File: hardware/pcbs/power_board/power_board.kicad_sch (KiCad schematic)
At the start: 5 parts, among them J1 Header_01x04

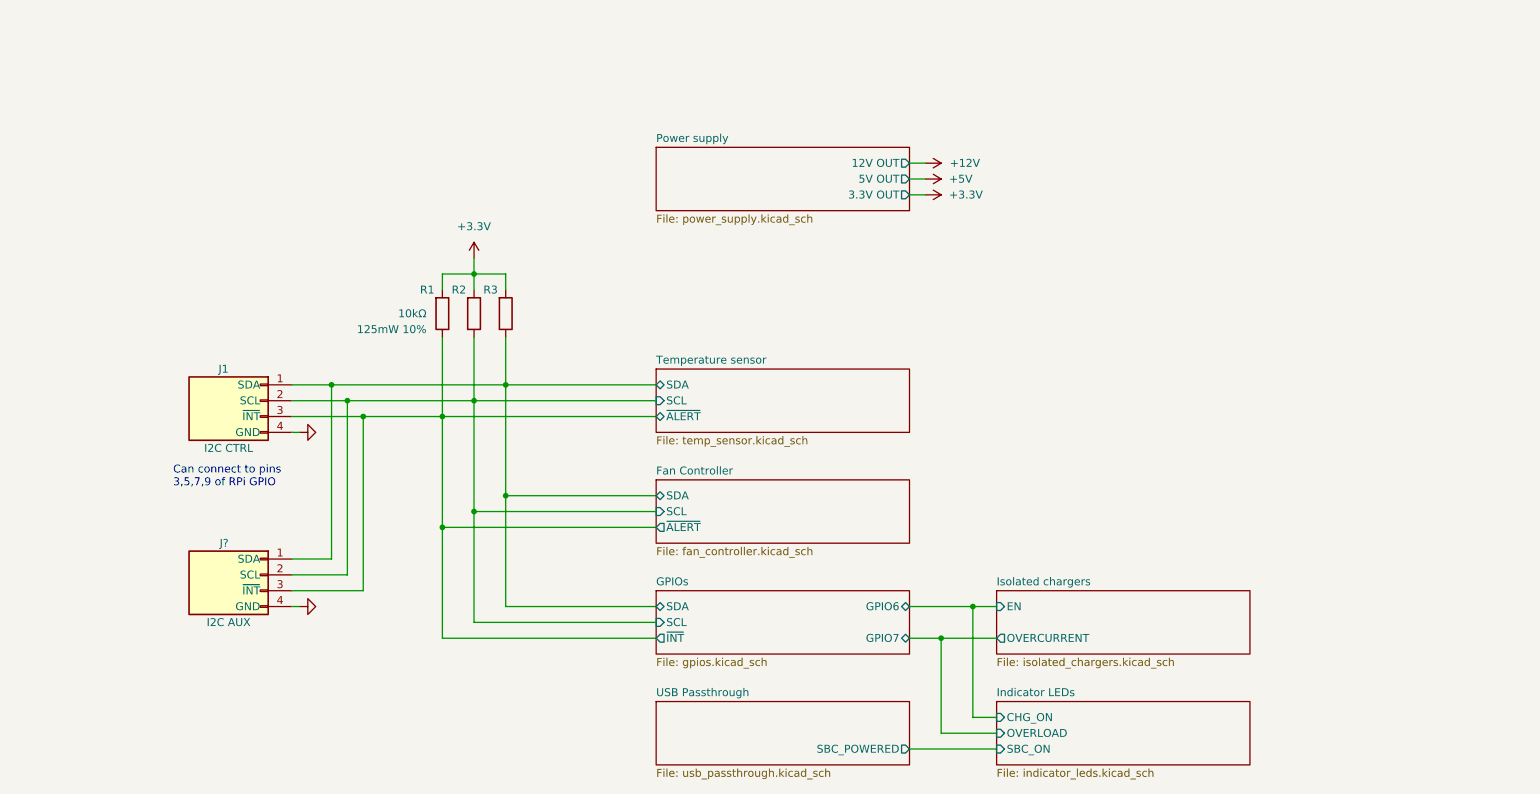
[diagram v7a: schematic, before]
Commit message: power_board: arrange front panel components
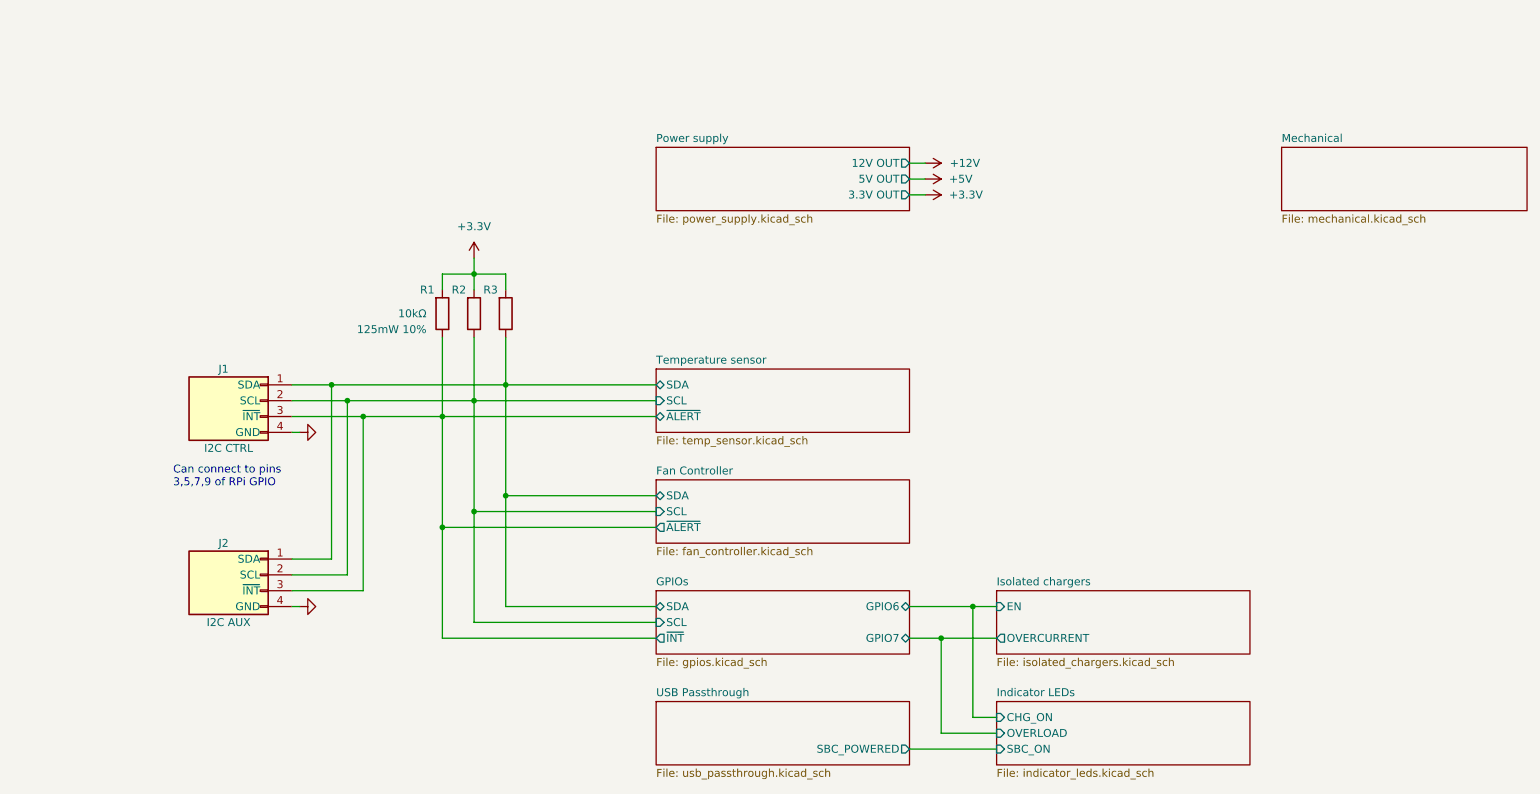
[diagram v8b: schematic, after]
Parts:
- gave numbers to parts that had none: 1
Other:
- added sheet Mechanical (mechanical.kicad_sch)
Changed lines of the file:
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@@
   (symbol (lib_id "power:+12V") (at 173.99 48.26 270) (unit 1)
     (in_bom yes) (on_board yes) (dnp no)
-    (property "Reference" "#PWR03" (at 170.18 48.26 0)
+    (property "Reference" "#PWR04" (at 170.18 48.26 0)
       (effects (font (size 1.27 1.27)) hide)
     )
@@
       (project "power_board"
         (path "/4b166175-80a4-48c6-994d-6e62a6160b87"
-          (reference "#PWR03") (unit 1)
+          (reference "#PWR04") (unit 1)
         )
       )
@@
   (symbol (lib_id "power:+3.3V") (at 173.99 53.34 270) (unit 1)
     (in_bom yes) (on_board yes) (dnp no) (fields_autoplaced)
-    (property "Reference" "#PWR05" (at 170.18 53.34 0)
+    (property "Reference" "#PWR06" (at 170.18 53.34 0)
       (effects (font (size 1.27 1.27)) hide)
     )
@@
       (project "power_board"
         (path "/4b166175-80a4-48c6-994d-6e62a6160b87"
+          (reference "#PWR06") (unit 1)
+        )
+      )
+    )
+  )
+  (symbol (lib_id "power:+5V") (at 173.99 50.8 270) (unit 1)
+    (in_bom yes) (on_board yes) (dnp no) (fields_autoplaced)
+    (property "Reference" "#PWR05" (at 170.18 50.8 0)
+      (effects (font (size 1.27 1.27)) hide)
+    )
+    (property "Value" "+5V" (at 177.8 50.8 90)
+      (effects (font (size 1.27 1.27)) (justify left))
+    )
+    (property "Footprint" "" (at 173.99 50.8 0)
+      (effects (font (size 1.27 1.27)) hide)
+    )
+    (property "Datasheet" "" (at 173.99 50.8 0)
+      (effects (font (size 1.27 1.27)) hide)
+    )
+    (pin "1")
+    (instances
+      (project "power_board"
+        (path "/4b166175-80a4-48c6-994d-6e62a6160b87"
           (reference "#PWR05") (unit 1)
-        )
-      )
-    )
-  )
-  (symbol (lib_id "power:+5V") (at 173.99 50.8 270) (unit 1)
-    (in_bom yes) (on_board yes) (dnp no) (fields_autoplaced)
-    (property "Reference" "#PWR04" (at 170.18 50.8 0)
-      (effects (font (size 1.27 1.27)) hide)
-    )
-    (property "Value" "+5V" (at 177.8 50.8 90)
-      (effects (font (size 1.27 1.27)) (justify left))
-    )
-    (property "Footprint" "" (at 173.99 50.8 0)
-      (effects (font (size 1.27 1.27)) hide)
-    )
-    (property "Datasheet" "" (at 173.99 50.8 0)
-      (effects (font (size 1.27 1.27)) hide)
-    )
-    (pin "1")
-    (instances
-      (project "power_board"
-        (path "/4b166175-80a4-48c6-994d-6e62a6160b87"
-          (reference "#PWR04") (unit 1)
         )
       )
@@
   (symbol (lib_id "conn:Conn_01x04") (at 67.31 114.3 0) (mirror y) (unit 1)
     (in_bom yes) (on_board yes) (dnp no)
-    (property "Reference" "J?" (at 62.23 109.22 0)
+    (property "Reference" "J2" (at 62.23 109.22 0)
       (effects (font (size 1.27 1.27)) (justify left))
     )
@@
       (project "power_board"
         (path "/4b166175-80a4-48c6-994d-6e62a6160b87"
-          (reference "J?") (unit 1)
+          (reference "J2") (unit 1)
         )
       )
@@
   (symbol (lib_id "power:+3.3V") (at 101.6 63.5 0) (unit 1)
     (in_bom yes) (on_board yes) (dnp no) (fields_autoplaced)
-    (property "Reference" "#PWR02" (at 101.6 67.31 0)
+    (property "Reference" "#PWR03" (at 101.6 67.31 0)
       (effects (font (size 1.27 1.27)) hide)
     )
@@
       (project "power_board"
         (path "/4b166175-80a4-48c6-994d-6e62a6160b87"
+          (reference "#PWR03") (unit 1)
+        )
+      )
+    )
+  )
+  (symbol (lib_id "power:GND") (at 73.66 119.38 90) (unit 1)
+    (in_bom yes) (on_board yes) (dnp no) (fields_autoplaced)
+    (property "Reference" "#PWR02" (at 80.01 119.38 0)
+      (effects (font (size 1.27 1.27)) hide)
+    )
+    (property "Value" "GND" (at 78.74 119.38 0)
+      (effects (font (size 1.27 1.27)) hide)
+    )
+    (property "Footprint" "" (at 73.66 119.38 0)
+      (effects (font (size 1.27 1.27)) hide)
+    )
+    (property "Datasheet" "" (at 73.66 119.38 0)
+      (effects (font (size 1.27 1.27)) hide)
+    )
+    (pin "1")
+    (instances
+      (project "power_board"
+        (path "/4b166175-80a4-48c6-994d-6e62a6160b87"
           (reference "#PWR02") (unit 1)
         )
@@
     )
   )
-  (symbol (lib_id "power:GND") (at 73.66 119.38 90) (unit 1)
-    (in_bom yes) (on_board yes) (dnp no) (fields_autoplaced)
-    (property "Reference" "#PWR0105" (at 80.01 119.38 0)
-      (effects (font (size 1.27 1.27)) hide)
-    )
-    (property "Value" "GND" (at 78.74 119.38 0)
-      (effects (font (size 1.27 1.27)) hide)
-    )
-    (property "Footprint" "" (at 73.66 119.38 0)
-      (effects (font (size 1.27 1.27)) hide)
-    )
-    (property "Datasheet" "" (at 73.66 119.38 0)
-      (effects (font (size 1.27 1.27)) hide)
-    )
-    (pin "1")
-    (instances
-      (project "power_board"
-        (path "/4b166175-80a4-48c6-994d-6e62a6160b87"
-          (reference "#PWR0105") (unit 1)
-        )
-      )
-    )
-  )
   (symbol (lib_id "power:GND") (at 73.66 91.44 90) (unit 1)
     (in_bom yes) (on_board yes) (dnp no) (fields_autoplaced)
@@
       )
     )
+  )
+  (sheet (at 231.14 45.72) (size 39.37 10.16) (fields_autoplaced)
+    (stroke (width 0.1524) (type solid))
+    (fill (color 0 0 0 0.0000))
+    (property "Sheetname" "Mechanical" (at 231.14 45.0084 0)
+      (effects (font (size 1.27 1.27)) (justify left bottom))
+    )
+    (property "Sheetfile" "mechanical.kicad_sch" (at 231.14 56.4646 0)
+      (effects (font (size 1.27 1.27)) (justify left top))
+    )
+    (instances
+      (project "power_board"
+        (path "/4b166175-80a4-48c6-994d-6e62a6160b87" (page "13"))
+      )
+    )
